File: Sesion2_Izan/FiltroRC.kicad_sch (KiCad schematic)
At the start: 1 part, among them J101 Conn_01x02

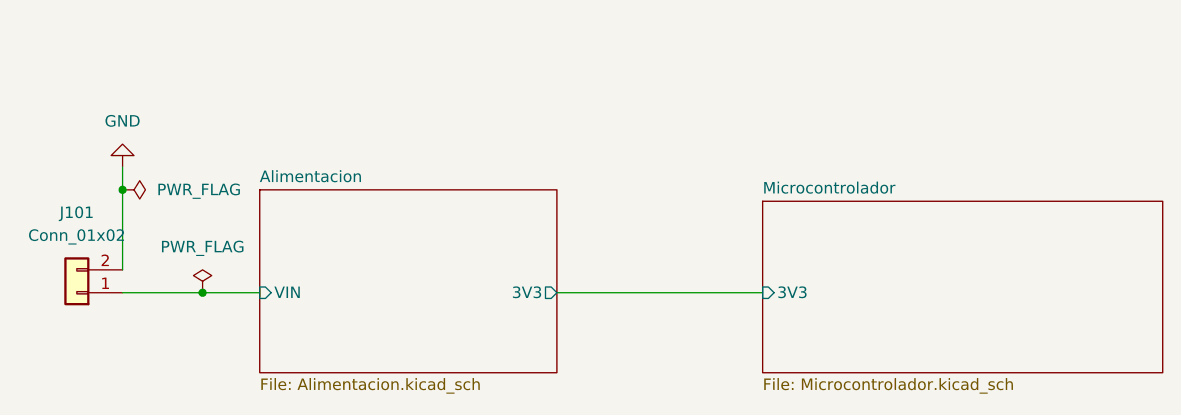
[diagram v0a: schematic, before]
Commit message: Complete microcontroller schematic and BOM
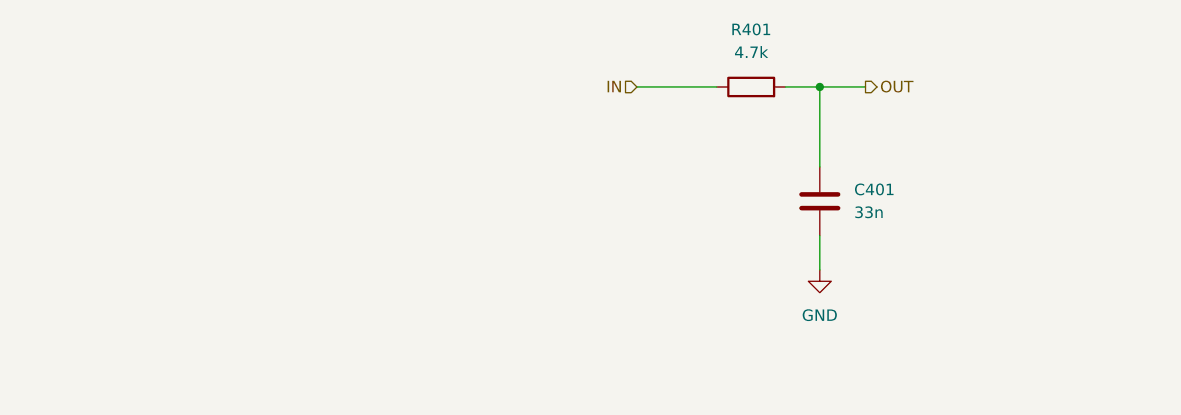
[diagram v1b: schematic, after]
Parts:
- removed J101: Conn_01x02, TerminalBlock_Phoenix:TerminalBlock_Phoenix_PT-1,5-2-5.0-H_1x02_P5.00mm_Horizontal, symbol Connector_Generic:Conn_01x02
- added C401: 33n, Capacitor_SMD:C_0805_2012Metric_Pad1.18x1.45mm_HandSolder, symbol Device:C
- added R401: 4.7k, Resistor_SMD:R_0805_2012Metric_Pad1.20x1.40mm_HandSolder, symbol Device:R
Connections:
- net GND: now also C401.2
- new net IN: R401.1
- new net OUT: C401.1, R401.2
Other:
- removed sheet Alimentacion
- removed sheet Microcontrolador
